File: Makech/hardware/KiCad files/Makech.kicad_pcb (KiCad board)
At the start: 2 copper layers, 54.9 x 88.5 mm, 52 parts, among them IC1 ULN2803, J1 SWD programmer, J2 USB_B_Micro, J3 ESP32-Exp, U1 ATSAMD21G18A-AU, U2 CONN_01X04, U3 AP2114_3.3v, X1 Screw_Terminal_1x02

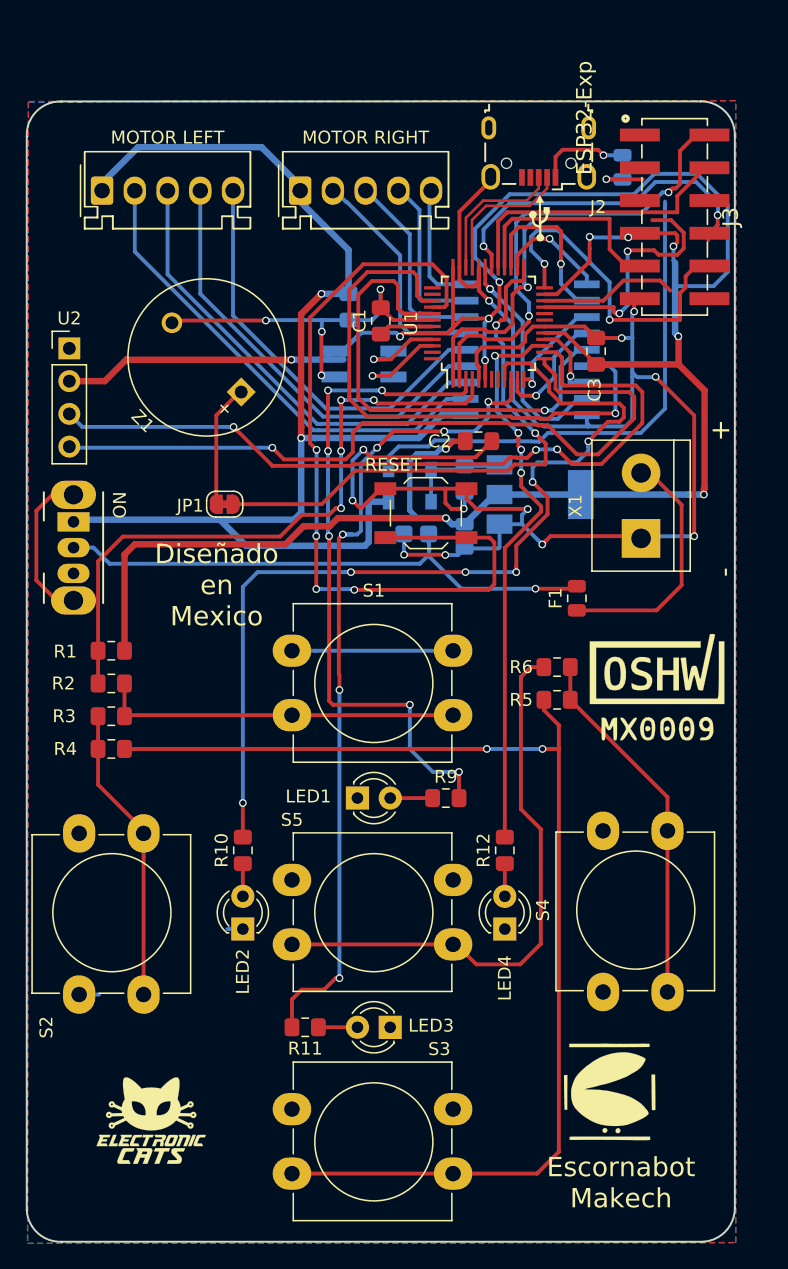
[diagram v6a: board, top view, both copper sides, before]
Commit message: Change routing and compnent placement v0.2
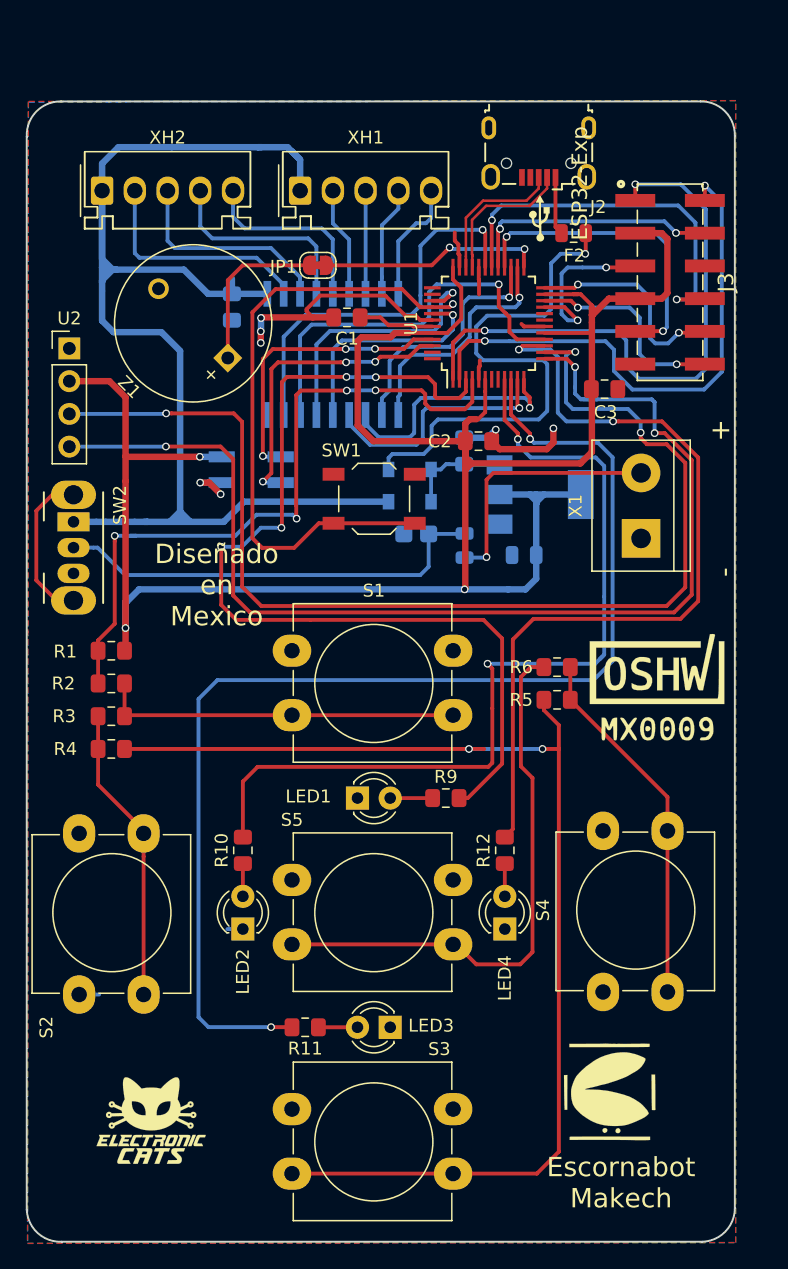
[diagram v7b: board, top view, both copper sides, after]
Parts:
- F1: moved to B.Cu
- F2: moved to F.Cu
- XH1: renamed from MOTOR RIGHT
- XH2: renamed from MOTOR LEFT
- moved JP1 19.9 mm to (120.1, 69.2)
- moved IC1 15.0 mm to (121.3, 76.1), turned to 90 degrees
- moved J1 12.0 mm to (115.0, 85.0)
- moved F1 9.62 mm to (131.5, 90.9)
- moved C6 9.05 mm to (113.5, 72.4)
- moved F2 6.36 mm to (140.0, 66.7), turned to 180 degrees
- moved J3 5.09 mm to (147.4, 70.5)
- moved C5 4.84 mm to (136.1, 91.6), turned to 180 degrees
- moved SW1 4.16 mm to (124.5, 87.3)
- moved C3 3.02 mm to (142.4, 78.8), turned to 0 degrees
- moved Z1 2.84 mm to (113.1, 76.4)
- moved C1 2.64 mm to (122.4, 73.2), turned to 180 degrees
- moved C4 2.18 mm to (131.5, 83.6), turned to 270 degrees
- renumbered RESET to SW1, ON to SW2
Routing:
- net GND: track 186.3 -> 43.5 mm, vias 16 -> 7
- net +3V3: track 207.2 -> 172.7 mm, vias 12 -> 3
- net /SCL: track 61.0 -> 90.7 mm
- net /SDA: track 60.0 -> 89.2 mm, vias 1 -> 3
- net /A2: track 65.6 -> 93.6 mm, vias 6 -> 2
- net /TX: track 18.6 -> 45.8 mm, vias 1 -> 2
- net /D10: track 43.9 -> 17.4 mm
- net /D3: track 6.08 -> 31.3 mm
- net /D4: track 44.4 -> 20.7 mm
- net /A0: track 52.6 -> 75.0 mm, vias 6 -> 4
- net /D5: track 38.0 -> 17.8 mm
- net /A3: track 44.3 -> 64.4 mm, vias 4 -> 2
- net /MR3: track 36.3 -> 16.6 mm
- net /MR4: track 37.7 -> 18.1 mm
- net /MR2: track 34.7 -> 16.1 mm
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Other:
- net class source: trace_width 0.3 -> 0.5

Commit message: Fix traces
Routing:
- net Net-(R4-Pad2): track 95.0 -> 90.6 mm
- net /A0: track 75.0 -> 75.9 mm
- net /A3: track 64.4 -> 65.2 mm
- net Net-(SW1-Pad2): track 48.2 -> 49.0 mm
- net /SDA: track 89.2 -> 89.8 mm
